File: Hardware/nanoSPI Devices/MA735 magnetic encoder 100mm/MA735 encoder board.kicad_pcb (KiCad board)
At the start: 2 copper layers, 5.7 x 80.4 mm, 4 parts, among them J1 FPC contacts 0.3mm, U1 MA735GGU-Z

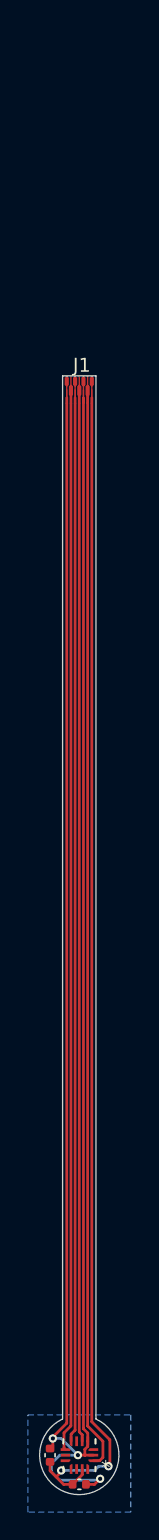
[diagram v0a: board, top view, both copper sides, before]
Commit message: Exported Gerbers for MA735 encoder
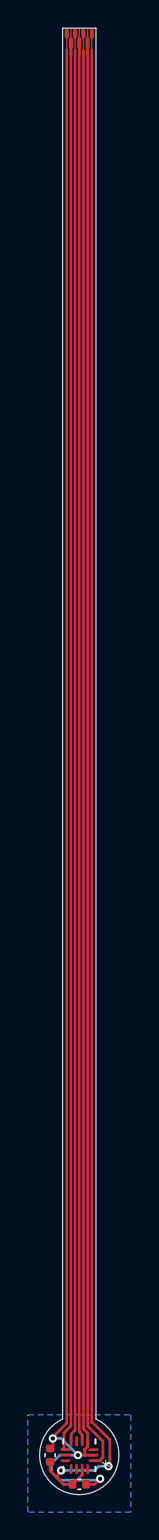
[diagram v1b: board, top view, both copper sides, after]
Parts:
- moved J1 25.0 mm to (152.8, 30.2)
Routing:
- net GND: track 164.8 -> 212.7 mm
- net /SCK: track 78.0 -> 103.0 mm
- net /MISO: track 75.7 -> 100.7 mm
- net /MOSI: track 76.5 -> 101.5 mm
- net /CS: track 75.7 -> 99.7 mm
- net +3V3: track 86.2 -> 110.2 mm
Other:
- board size 5.7 x 80.4 mm -> 5.7 x 105.4 mm
- board text added: "0.1mm thick stiffener"

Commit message: Updated files for JLC DFM checks
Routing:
- net GND: track 212.7 -> 204.0 mm
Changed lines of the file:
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@@
 		(start 153.2 131.7)
 		(end 152.9 131.7)
-		(width 0.2)
+		(width 0.16)
 		(layer "F.Cu")
 		(net 1)
@@
 		(start 153.28 133.8)
 		(end 153.9 133.8)
-		(width 0.2)
+		(width 0.16)
 		(layer "F.Cu")
 		(net 1)
@@
 		(start 152.9 131.7)
 		(end 152.7 131.7)
-		(width 0.2)
+		(width 0.16)
 		(layer "F.Cu")
 		(net 1)
@@
 		(start 153.2 131.277564)
 		(end 153.2 131.7)
-		(width 0.2)
+		(width 0.16)
 		(layer "F.Cu")
 		(net 1)
@@
 		(start 150.7 130.5)
 		(end 150.9 130.5)
-		(width 0.2)
+		(width 0.16)
 		(layer "F.Cu")
 		(net 1)
@@
 		(start 153.410408 130.7)
 		(end 153.410408 131.067156)
-		(width 0.2)
+		(width 0.16)
 		(layer "F.Cu")
 		(net 1)
@@
 		(start 153.810409 131.7)
 		(end 153.2 131.7)
-		(width 0.2)
+		(width 0.16)
 		(layer "F.Cu")
 		(net 1)
@@
 		(start 150.9 130.4)
 		(end 151.9 129.4)
-		(width 0.2)
+		(width 0.16)
 		(layer "F.Cu")
 		(net 1)
@@
 		(start 150.9 130.5)
 		(end 150.9 130.4)
-		(width 0.2)
+		(width 0.16)
 		(layer "F.Cu")
 		(net 1)
@@
 		(start 150.9 130.5)
 		(end 150.9 131.02)
-		(width 0.2)
+		(width 0.16)
 		(layer "F.Cu")
 		(net 1)
@@
 		(start 153.410408 130.7)
 		(end 153.410408 130.111414)
-		(width 0.2)
+		(width 0.16)
 		(layer "F.Cu")
 		(net 1)
@@
 		(start 153.410408 130.111414)
 		(end 153.1 129.801006)
-		(width 0.2)
+		(width 0.16)
 		(layer "F.Cu")
 		(net 1)
@@
 		(start 153.410408 131.067156)
 		(end 153.2 131.277564)
-		(width 0.2)
+		(width 0.16)
 		(layer "F.Cu")
 		(net 1)
@@
 		(start 150.9 131.02)
 		(end 150.7 131.22)
-		(width 0.2)
+		(width 0.16)
 		(layer "F.Cu")
 		(net 1)
@@
 		(start 153.9 133.8)
 		(end 154.3 133.4)
-		(width 0.2)
+		(width 0.16)
 		(layer "F.Cu")
 		(net 1)
@@
 		(start 153.1 129.801006)
 		(end 153.1 31.120336)
-		(width 0.2)
+		(width 0.16)
 		(layer "F.Cu")
 		(net 1)
@@
 		(start 151.9 129.4)
 		(end 151.9 31.120336)
-		(width 0.2)
+		(width 0.16)
 		(layer "F.Cu")
 		(net 1)
@@
 		(drill 0.3)
 		(layers "F.Cu" "B.Cu")
-		(net 1)
-	)
-	(segment
-		(start 150.9 130.5)
-		(end 151.5 130.5)
-		(width 0.2)
-		(layer "B.Cu")
 		(net 1)
 	)
@@
 	)
 	(segment
-		(start 151.5 130.5)
-		(end 152.7 131.7)
-		(width 0.2)
-		(layer "B.Cu")
-		(net 1)
-	)
-	(segment
-		(start 150.8 132.3)
-		(end 151.4 131.7)
-		(width 0.2)
-		(layer "B.Cu")
-		(net 1)
-	)
-	(segment
-		(start 151.4 131.7)
-		(end 152.7 131.7)
-		(width 0.2)
-		(layer "B.Cu")
-		(net 1)
-	)
-	(segment
-		(start 150.8 132.9)
-		(end 150.8 132.3)
-		(width 0.2)
-		(layer "B.Cu")
-		(net 1)
-	)
-	(segment
-		(start 151.4 133.5)
-		(end 150.8 132.9)
-		(width 0.2)
-		(layer "B.Cu")
-		(net 1)
-	)
-	(segment
-		(start 154.2 133.5)
-		(end 151.4 133.5)
-		(width 0.2)
-		(layer "B.Cu")
-		(net 1)
-	)
-	(segment
 		(start 155 130.6)
 		(end 153.7 129.3)
-		(width 0.2)
+		(width 0.16)
 		(layer "F.Cu")
 		(net 2)
@@
 		(start 154.9 132.5)
 		(end 155 132.4)
-		(width 0.2)
+		(width 0.16)
 		(layer "F.Cu")
 		(net 2)
@@
 		(start 155 132.4)
 		(end 155 130.6)
-		(width 0.2)
+		(width 0.16)
 		(layer "F.Cu")
 		(net 2)
@@
 		(start 152.32 133.8)
 		(end 151.673449 133.8)
-		(width 0.2)
+		(width 0.16)
 		(layer "F.Cu")
 		(net 2)
@@
 		(start 153.7 129.3)
 		(end 153.7 31.120336)
-		(width 0.2)
+		(width 0.16)
 		(layer "F.Cu")
 		(net 2)
@@
 		(start 153.010408 132.700001)
 		(end 153.010408 133.109592)
-		(width 0.2)
+		(width 0.16)
 		(layer "F.Cu")
 		(net 2)
@@
 		(start 151.5 132.9)
 		(end 151.136724 133.263276)
-		(width 0.2)
+		(width 0.16)
 		(layer "F.Cu")
 		(net 2)
@@
 		(start 151.136724 133.263276)
 		(end 150.7 132.826551)
-		(width 0.2)
+		(width 0.16)
 		(layer "F.Cu")
 		(net 2)
@@
 		(start 150.7 132.826551)
 		(end 150.7 132.18)
-		(width 0.2)
+		(width 0.16)
 		(layer "F.Cu")
 		(net 2)
@@
 		(start 151.5 132.8)
 		(end 151.5 132.9)
-		(width 0.2)
+		(width 0.16)
 		(layer "F.Cu")
 		(net 2)
@@
 		(start 153.010408 133.109592)
 		(end 152.32 133.8)
-		(width 0.2)
+		(width 0.16)
 		(layer "F.Cu")
 		(net 2)
@@
 		(start 151.673449 133.8)
 		(end 151.136724 133.263276)
-		(width 0.2)
+		(width 0.16)
 		(layer "F.Cu")
 		(net 2)
@@
 		(start 153.9 132.8)
 		(end 151.5 132.8)
-		(width 0.2)
+		(width 0.16)
 		(layer "B.Cu")
 		(net 2)
@@
 		(start 154.2 132.5)
 		(end 153.9 132.8)
-		(width 0.2)
+		(width 0.16)
 		(layer "B.Cu")
 		(net 2)
@@
 		(start 154.9 132.5)
 		(end 154.2 132.5)
-		(width 0.2)
+		(width 0.16)
 		(layer "B.Cu")
 		(net 2)
@@
 		(start 151.7 131.189593)
 		(end 151.810408 131.300001)
-		(width 0.2)
+		(width 0.16)
 		(layer "F.Cu")
 		(net 3)
@@
 		(start 152.2 129.6)
 		(end 151.7 130.1)
-		(width 0.2)
+		(width 0.16)
 		(layer "F.Cu")
 		(net 3)
@@
 		(start 152.2 30.1)
 		(end 152.2 129.6)
-		(width 0.2)
+		(width 0.16)
 		(layer "F.Cu")
 		(net 3)
@@
 		(start 151.7 130.1)
 		(end 151.7 131.189593)
-		(width 0.2)
+		(width 0.16)
 		(layer "F.Cu")
 		(net 3)
@@
 		(start 152.8 30.1)
 		(end 152.8 130.026276)
-		(width 0.2)
+		(width 0.16)
 		(layer "F.Cu")
 		(net 4)
@@
 		(start 153.010408 130.236684)
 		(end 153.010408 130.699999)
-		(width 0.2)
+		(width 0.16)
 		(layer "F.Cu")
 		(net 4)
@@
 		(start 152.8 130.026276)
 		(end 153.010408 130.236684)
-		(width 0.2)
+		(width 0.16)
 		(layer "F.Cu")
 		(net 4)
@@
 		(start 152.210409 130.189591)
 		(end 152.5 129.9)
-		(width 0.2)
+		(width 0.16)
 		(layer "F.Cu")
 		(net 5)
@@
 		(start 152.5 129.9)
 		(end 152.5 31.120336)
-		(width 0.2)
+		(width 0.16)
 		(layer "F.Cu")
 		(net 5)
@@
 		(start 152.210409 130.7)
 		(end 152.210409 130.189591)
-		(width 0.2)
+		(width 0.16)
 		(layer "F.Cu")
 		(net 5)
@@
 		(start 154.5 130.7)
 		(end 153.4 129.6)
-		(width 0.2)
+		(width 0.16)
 		(layer "F.Cu")
 		(net 6)
@@
 		(start 153.810408 132.1)
 		(end 154.260409 132.1)
-		(width 0.2)
+		(width 0.16)
 		(layer "F.Cu")
 		(net 6)
@@
 		(start 154.5 131.860409)
 		(end 154.5 130.7)
-		(width 0.2)
+		(width 0.16)
 		(layer "F.Cu")
 		(net 6)
@@
 		(start 153.4 129.6)
 		(end 153.4 30.1)
-		(width 0.2)
+		(width 0.16)
 		(layer "F.Cu")
 		(net 6)
@@
 		(start 154.260409 132.1)
 		(end 154.5 131.860409)
-		(width 0.2)
-		(layer "F.Cu")
-		(net 6)
+		(width 0.16)
+		(layer "F.Cu")
+		(net 6)
